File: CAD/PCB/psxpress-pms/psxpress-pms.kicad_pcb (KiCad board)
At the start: 2 copper layers, 29.7 x 24.1 mm, 44 parts, among them IC1 BQ25606RGER, IC2 MAX16054AZT+T, IC3 TPS61023DRLT, IC4 TPS564255DRLR, Q1 AONR21117, SW1 SW_SPST

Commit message: pms - update 3v5 regulator symbol & fix routing, symbol was incorrect
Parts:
- removed the REF** at (175.9, 79.1)
- moved C13 7.05 mm to (185.6, 75.3), turned to 90 degrees
- moved C14 5.21 mm to (183.5, 75.3), turned to 90 degrees
- moved C12 4.90 mm to (176.7, 69.0), turned to 0 degrees
- moved R9 4.35 mm to (181.7, 72.2), turned to 90 degrees
- moved L3 3.40 mm to (180.1, 76.0), turned to 0 degrees
- moved R10 2.06 mm to (180.1, 72.2), turned to -90 degrees
- moved IC4 0.68 mm to (178.0, 72.2), turned to 90 degrees
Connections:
- IC4 pad 1: Net-(IC4-FB) -> VSYS
- IC4 pad 2: VSYS -> Net-(IC4-SW)
- IC4 pad 3: VSYS -> GND
- IC4 pad 4: GND -> unconnected-(IC4-PG-Pad4)
- IC4 pad 5: Net-(IC4-SW) -> VSYS
- IC4 pad 6: unconnected-(IC4-PG-Pad6) -> Net-(IC4-FB)
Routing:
- net +3.5V: track 13.3 -> 0.00 mm, vias 2 -> 0
- net Net-(IC4-FB): track 4.00 -> 5.39 mm
- net GND: track 1.33 -> 1.11 mm, vias 78 -> 72

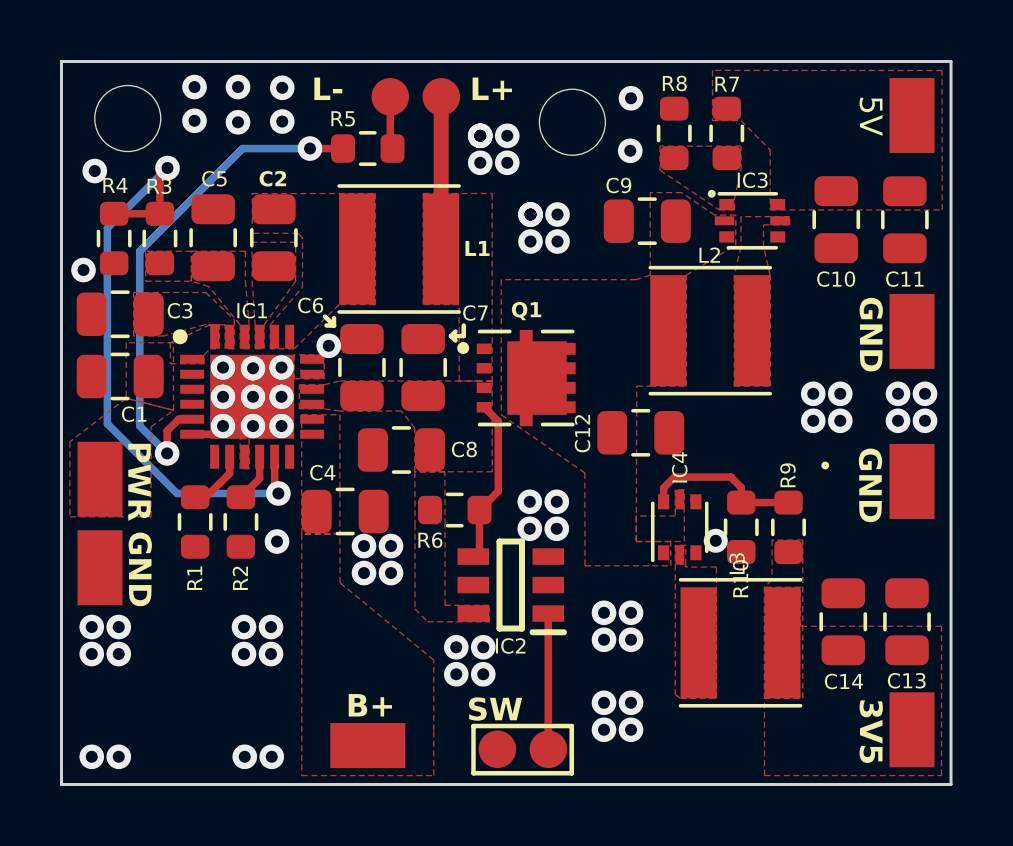
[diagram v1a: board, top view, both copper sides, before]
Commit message: pms - finish routing new regs + POR circuit - add special thanks - awaiting cleanup
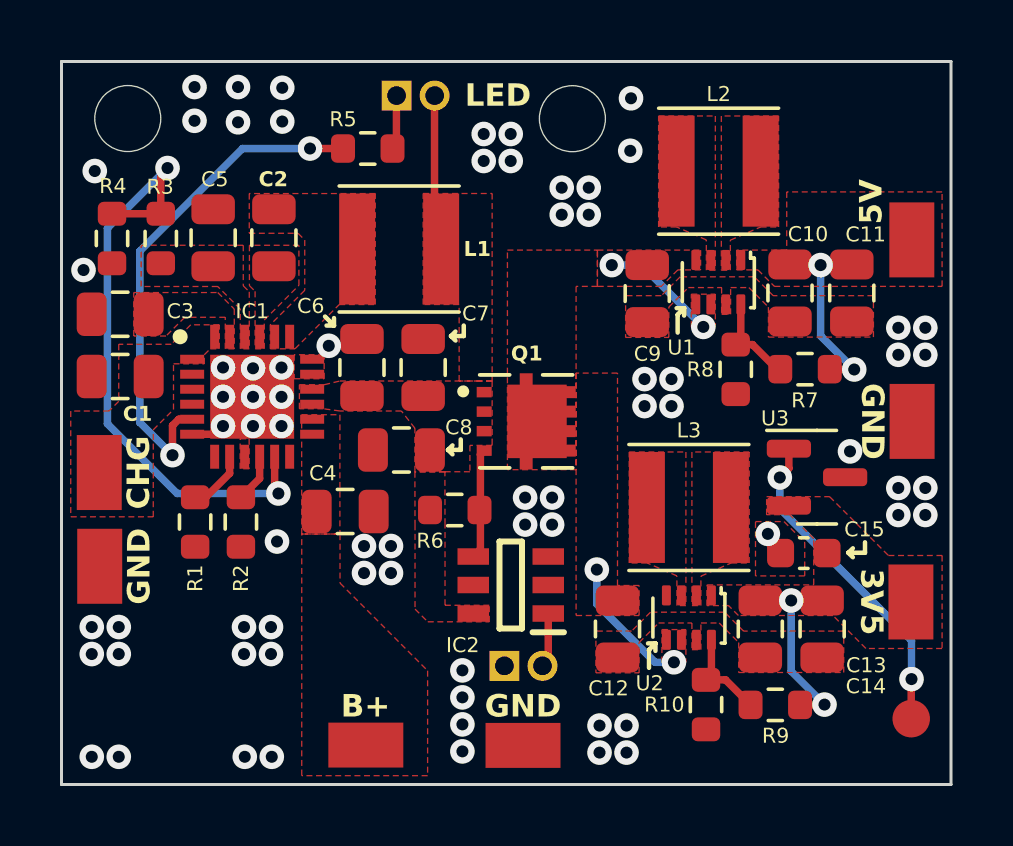
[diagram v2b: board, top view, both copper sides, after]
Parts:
- removed IC3: TPS61023DRLT, Package_TO_SOT_SMD:SOT-666
- removed IC4: TPS564255DRLR, Package_TO_SOT_SMD:SOT-666
- added C15: 100nF, Capacitor_SMD:C_0603_1608Metric, F.Cu at (182.2, 73.1)
- added TP4: GND, solderpads:hipower_2.5x1.5mm, F.Cu at (185.8, 68.7)
- added U1: TPS631000, Package_TO_SOT_SMD:SOT-583-8, F.Cu at (179.3, 64.0)
- added U2: TPS631000, Package_TO_SOT_SMD:SOT-583-8, F.Cu at (178.3, 75.2)
- added U3: MCP120-315I, Package_TO_SOT_SMD:SOT-23, F.Cu at (182.6, 70.5)
- IC1: value BQ25606RGER -> BQ25606
- IC2: value MAX16054AZT+T -> MAX16054
- R7: value 750k -> 909k
- R9: value 487k -> 604k
- TP6: value +3V5 -> +5V
- TP8: value GND -> RST; footprint solderpads:hipower_2.5x1.5mm -> solderpads:lopower_1.25mm
- moved TP7 18.9 mm to (172.8, 79.5), turned to 0 degrees
- moved R7 8.28 mm to (182.2, 66.9), turned to 180 degrees
- moved R8 8.13 mm to (179.9, 66.9), turned to -90 degrees
- moved TP8 7.86 mm to (185.7, 78.6)
- moved C12 6.59 mm to (175.9, 75.6), turned to -90 degrees
- moved R10 6.03 mm to (178.9, 78.1)
- moved R9 5.94 mm to (181.2, 78.1), turned to 180 degrees
- moved L2 5.32 mm to (179.3, 60.3)
- moved C13 4.90 mm to (180.7, 75.6), turned to -90 degrees
- moved L3 4.83 mm to (178.3, 71.5)
- moved TP6 4.31 mm to (185.7, 74.7), turned to 90 degrees
- moved TP5 4.10 mm to (185.8, 62.6), turned to 90 degrees
- moved C11 3.01 mm to (183.8, 64.4)
- moved C10 2.89 mm to (181.7, 64.4)
- moved SW1 2.73 mm to (172.8, 76.8)
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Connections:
- L2 pad 1: VSYS -> Net-(U1-LX1)
- L3 pad 2: +3.5V -> Net-(U2-LX2)
- TP8 pad 1: GND -> RST
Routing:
- net RST: track 0.00 -> 10.9 mm, vias 0 -> 2
- net VSYS: track 0.00 -> 8.43 mm, vias 0 -> 4
- net +5V: track 0.00 -> 4.76 mm, vias 0 -> 2
- net +3.5V: track 0.00 -> 4.75 mm, vias 0 -> 2
- net Net-(U1-FB): track 0.00 -> 3.24 mm
- net Net-(IC2-IN): track 4.53 -> 1.82 mm
- net Net-(U2-FB): track 5.39 -> 3.24 mm
- net Net-(IC2-~{OUT}): track 5.51 -> 3.71 mm
- net GND: vias 72 -> 71
- added copper zone on F.Cu, net Net-(U1-LX1)
- added copper zone on F.Cu, net Net-(U2-LX2)
- removed copper zone on F.Cu, net Net-(U1-FB)
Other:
- board text added: "LED"
- board text added: "Special thanks to these communities: BitBuilt PSX.Dev ReSwitched Thank you for your interest & support!"
- board text removed: "3V5"
- board text removed: "5V"
- board text removed: "B+"
- board text removed: "GND"
- board text removed: "L+"
- board text removed: "L-"
- board text removed: "PWR"
- board text removed: "SW"

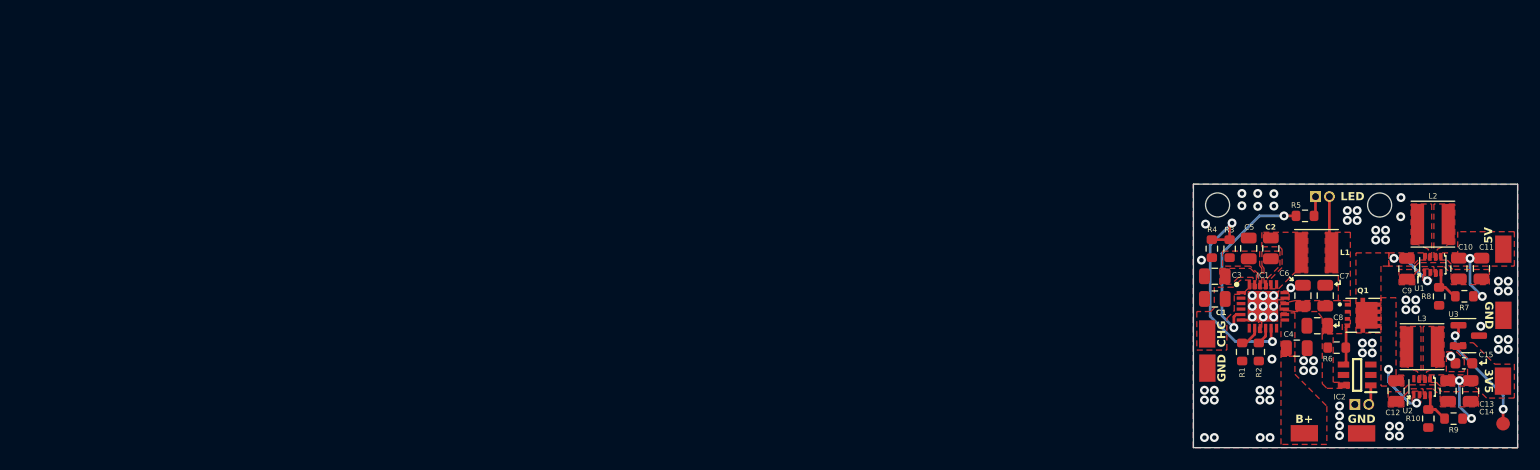
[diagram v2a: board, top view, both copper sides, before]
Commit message: pms - route reverse polarity protection circuit, finish cleanup
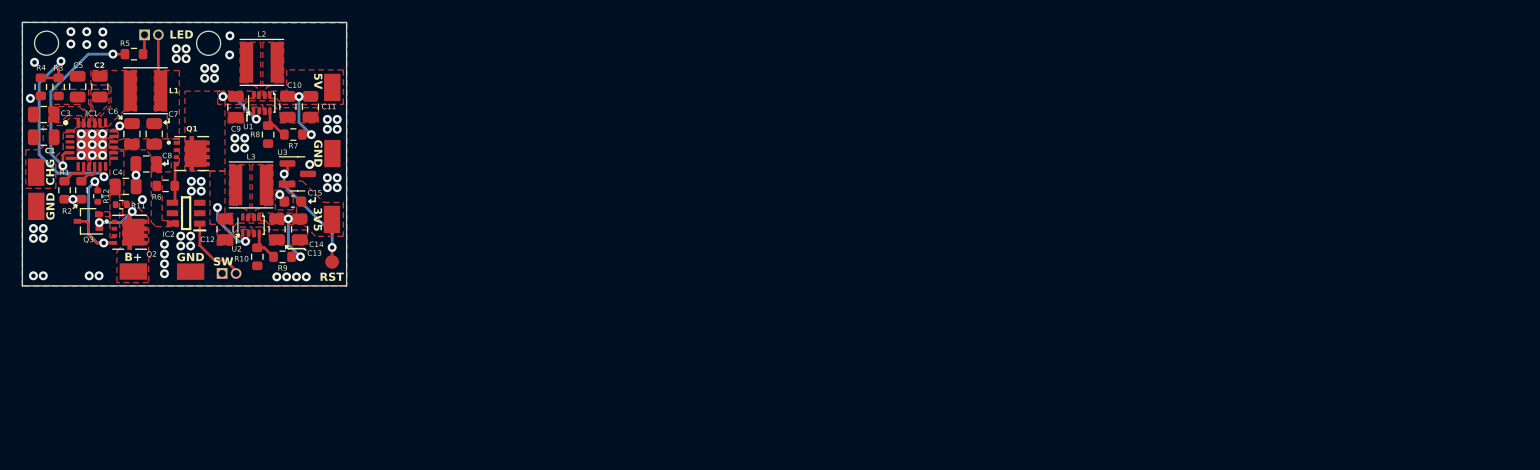
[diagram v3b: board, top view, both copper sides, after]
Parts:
- added Q2: AONR21117, TRANS_AONR21321:TRANS_AONR21321, F.Cu at (60.1, 61.1)
- added Q3: SI1317DL-T1-GE3, Package_TO_SOT_SMD:SOT-323_SC-70, F.Cu at (56.3, 60.1)
- added R11: 100k, Resistor_SMD:R_0402_1005Metric, F.Cu at (59.3, 58.5)
- added R12: 100k, Resistor_SMD:R_0402_1005Metric, F.Cu at (57.2, 57.8)
- TP3: value BAT -> B+
- moved R1 108.7 mm to (54.2, 57.2)
- moved R2 108.7 mm to (55.7, 57.2)
- moved C13 108.1 mm to (73.6, 60.8)
- moved C14 108.1 mm to (75.7, 60.8)
- moved IC2 108.1 mm to (65.3, 59.3)
- moved L1 108.1 mm to (61.6, 48.1)
- moved L3 108.1 mm to (71.2, 56.7)
- moved R10 108.1 mm to (71.8, 63.3)
- moved R9 108.1 mm to (74.1, 63.3)
- moved TP2 108.1 mm to (51.6, 55.6)
- moved TP4 108.1 mm to (78.7, 53.9)
- moved TP7 108.1 mm to (65.7, 64.7)
- moved TP8 108.1 mm to (78.6, 63.8)
- moved U2 108.1 mm to (71.2, 60.4)
- moved C1 108.1 mm to (52.3, 52.4)
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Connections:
- C4 pad 1: Net-(C4-Pad1) -> BAT
- IC1 pad 13: Net-(C4-Pad1) -> BAT
- IC1 pad 14: Net-(C4-Pad1) -> BAT
- TP3 pad 1: Net-(C4-Pad1) -> Net-(Q3-G)
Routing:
- net Net-(Q2-G): track 0.00 -> 13.4 mm, vias 0 -> 2
- net Net-(IC2-IN): track 1.82 -> 6.52 mm
- net Net-(Q3-G): track 0.00 -> 4.24 mm, vias 0 -> 2
- net Net-(IC1-ILIM): track 2.03 -> 2.63 mm
- net GND: vias 71 -> 69
- added copper zone on F.Cu, net BAT
- added copper zone on F.Cu, net Net-(Q3-G)
- removed copper zone on F.Cu, net Net-(C4-Pad1)
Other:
- board text added: "${CURRENT_DATE}"
- board text added: "PSXpress Power Management System"
- board text added: "RST"
- board text added: "SW"

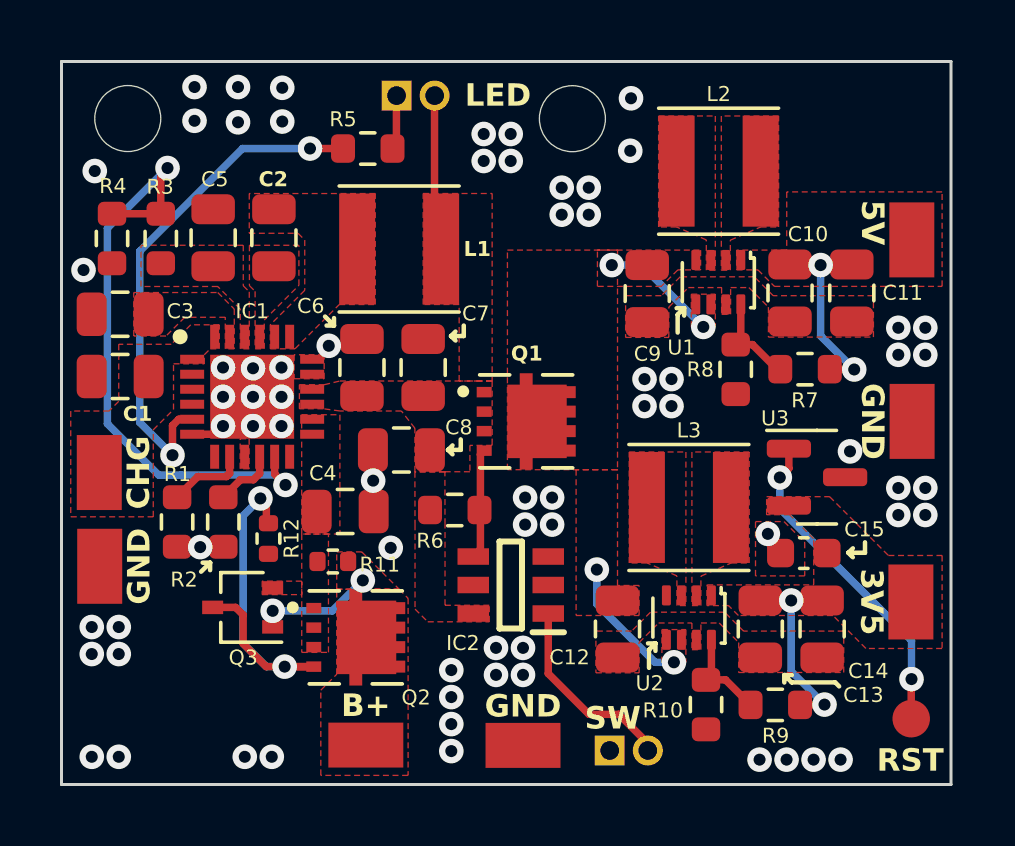
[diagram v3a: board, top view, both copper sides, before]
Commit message: pms - clear all DRC errors, further cleanup
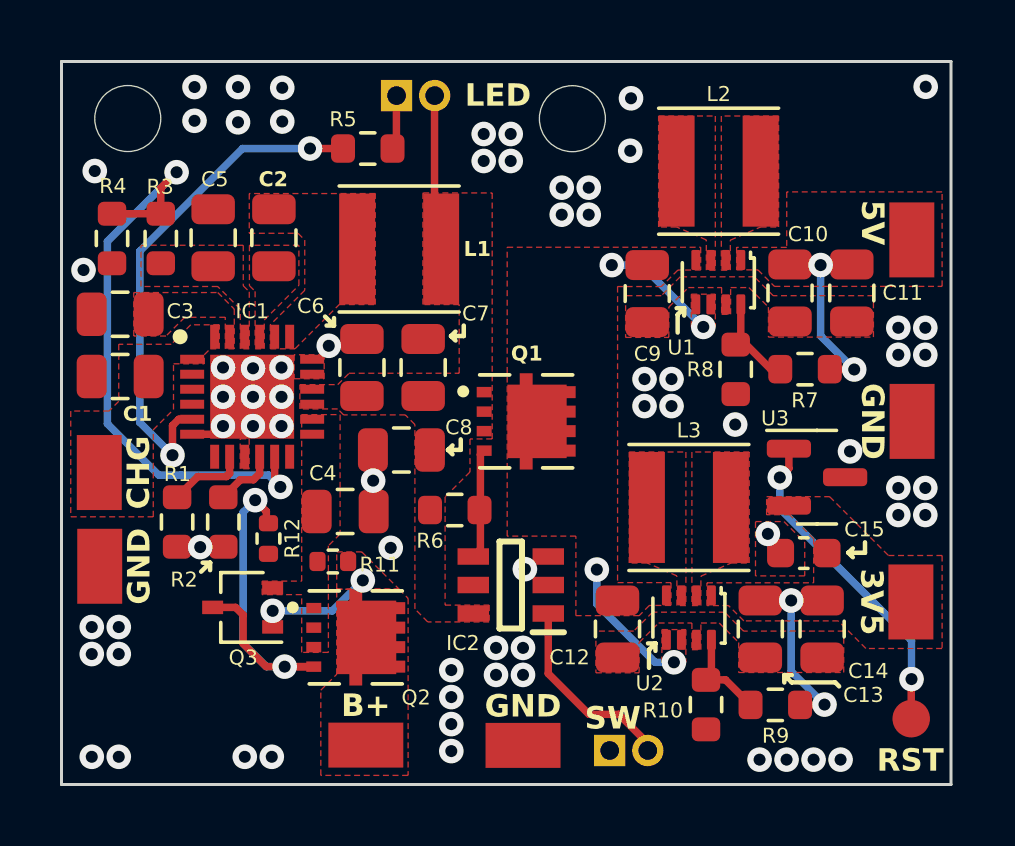
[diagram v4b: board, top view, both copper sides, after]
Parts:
- Q3: value SI1317DL-T1-GE3 -> SI1317DL
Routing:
- net GND: vias 69 -> 68
